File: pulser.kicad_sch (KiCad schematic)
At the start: 49 parts, among them J10 CONSMA002-SMD, J3 CONSMA002-SMD, J4 CONSMA002-SMD, J5 CONSMA002-SMD, J6 CONSMA002-SMD, J7 CONSMA002-SMD, J8 CONSMA002-SMD, J9 CONSMA002-SMD, U10 TLV9354IDR, U11 TLV9354IDR, U2 DSC1001DI2-125.0000T, U3 MAX14808ETK_

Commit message: DONE (inshallah)
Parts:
- added J16: External Power Connector, symbol Connector_Generic:Conn_02x08_Odd_Even
- added R128, R129, R130, R131, R132, R133, R134, R135: 90R 0805, symbol Device:R
- added TP1, TP2, TP3, TP4, TP5, TP53, TP54, TP55, TP56, TP57, TP58, TP59, TP6, TP60, TP7, TP8: RCT-0C, digikey-footprints:PROBE_PAD_0805, symbol dk_Test-Points:RCT-0C
- added TP10, TP11, TP12, TP13, TP14, TP15, TP16, TP9: TestPoint, symbol Connector:TestPoint
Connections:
- net TR_OUT1: now also R132.2; no longer R83.2, R84.1, U10.1 (OUT_A), U3.1 (LVOUT1)
- net TR_OUT2: now also R130.2; no longer R85.2, R86.1, U10.7 (OUT_B), U3.2 (LVOUT2)
- net TR_OUT3: now also R131.1; no longer R88.2, R90.1, U10.8 (OUT_C), U3.3 (LVOUT3)
- net TR_OUT4: now also R133.1; no longer R87.2, R89.1, U10.14 (OUT_D), U3.4 (LVOUT4)
- net TR_OUT5: now also R134.2; no longer R91.2, R93.1, U11.1 (OUT_A), U3.14 (LVOUT5)
- net TR_OUT6: now also R128.2; no longer R92.2, R94.1, U11.7 (OUT_B), U3.15 (LVOUT6)
- net TR_OUT7: now also R129.1; no longer R96.1, R98.2, U11.8 (OUT_C), U3.16 (LVOUT7)
- net TR_OUT8: now also R135.1; no longer R95.1, R97.2, U11.14 (OUT_D), U3.17 (LVOUT8)
- net VGNA: now also J16.1 (Pin_1), J16.2 (Pin_2), TP16.1
- net VGNB: now also J16.15 (Pin_15), J16.16 (Pin_16), TP9.1
- net VGPA: now also J16.3 (Pin_3), J16.4 (Pin_4), TP15.1
- net VGPB: now also J16.13 (Pin_13), J16.14 (Pin_14), TP10.1
- net VNNA: now also J16.7 (Pin_7), J16.8 (Pin_8), TP13.1
- net VNNB: now also J16.10 (Pin_10), J16.9 (Pin_9), TP12.1
- net VPPA: now also J16.5 (Pin_5), J16.6 (Pin_6), TP14.1
- net VPPB: now also J16.11 (Pin_11), J16.12 (Pin_12), TP11.1
- new net: R135.2, R95.1, TP58.1, U11.14 (OUT_D)
- new net: R130.1, R86.1, TP55.1, U10.7 (OUT_B)
- new net: R134.1, R93.1, TP57.1, U11.1 (OUT_A)
- new net: R133.2, R89.1, TP54.1, U10.14 (OUT_D)
- new net: R132.1, R84.1, TP53.1, U10.1 (OUT_A)
- new net: R131.2, R90.1, TP56.1, U10.8 (OUT_C)
- new net: R128.1, R94.1, TP59.1, U11.7 (OUT_B)
- new net: R129.2, R96.1, TP60.1, U11.8 (OUT_C)
- new net TR1: R83.2, TP1.1, U3.1 (LVOUT1)
- new net TR2: R85.2, TP2.1, U3.2 (LVOUT2)
- new net TR3: R88.2, TP3.1, U3.3 (LVOUT3)
- new net TR4: R87.2, TP4.1, U3.4 (LVOUT4)
- new net TR5: R91.2, TP5.1, U3.14 (LVOUT5)
- new net TR6: R92.2, TP6.1, U3.15 (LVOUT6)
- new net TR7: R98.2, TP7.1, U3.16 (LVOUT7)
- new net TR8: R97.2, TP8.1, U3.17 (LVOUT8)

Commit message: started layout, 20-30% done
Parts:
- added J18, J19, J20, J21, J22, J23, J24, J25: Conn_01x02_Pin, Connector_PinHeader_2.54mm:PinHeader_1x02_P2.54mm_Vertical, symbol Connector:Conn_01x02_Pin
- C1, C10, C11, C12, C2, C3, C4, C5, C6, C7, C8, C85, C86, C9: footprint (none) -> Capacitor_SMD:C_0603_1608Metric
- J16: footprint (none) -> Connector_PinHeader_2.54mm:PinHeader_2x08_P2.54mm_Vertical
- JP1, JP2, JP3, JP7: footprint (none) -> Jumper:SolderJumper-3_P1.3mm_Open_Pad1.0x1.5mm
- R128, R129, R130, R131, R132, R133, R134, R135, R48, R49, R50, R83, R84, R85, R86, R87, R88, R89, R90, R91, R92, R93, R94, R95, R96, R97, R98: footprint (none) -> Resistor_SMD:R_0603_1608Metric
- TP10, TP11, TP12, TP13, TP14, TP15, TP16, TP9: footprint (none) -> TestPoint:TestPoint_Pad_D1.5mm
- U10, U11: footprint SOIC_9354IDR_TEX -> TLV9354IDR:SOIC_9354IDR_TEX
- U2: footprint CDFN4_2P5X2_MCH -> DSC1001DI2-125.0000T:CDFN4_2P5X2_MCH
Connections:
- net GND: now also J18.2 (Pin_2), J19.2 (Pin_2), J20.2 (Pin_2), J21.2 (Pin_2), J22.2 (Pin_2), J23.2 (Pin_2), J24.2 (Pin_2), J25.2 (Pin_2)
- net HV_OUT3: now reaches J5.1, U3.47 (OUT3)
- net HV_OUT3: now also J20.1 (Pin_1)
- net HV_OUT1: now reaches J3.1, U3.51 (OUT1)
- net HV_OUT1: now also J18.1 (Pin_1)
- net HV_OUT2: now reaches J4.1, U3.49 (OUT2)
- net HV_OUT2: now also J19.1 (Pin_1)
- net HV_OUT6: now reaches J8.1, U3.39 (OUT6)
- net HV_OUT6: now also J23.1 (Pin_1)
- net HV_OUT8: now reaches J10.1, U3.35 (OUT8)
- net HV_OUT8: now also J25.1 (Pin_1)
- net HV_OUT7: now reaches J9.1, U3.37 (OUT7)
- net HV_OUT7: now also J24.1 (Pin_1)
- net HV_OUT5: now reaches J7.1, U3.41 (OUT5)
- net HV_OUT5: now also J22.1 (Pin_1)
- net HV_OUT4: now reaches J6.1, U3.45 (OUT4)
- net HV_OUT4: now also J21.1 (Pin_1)
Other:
- moved on the sheet: J10, J3, J4, J5, J6, J7, J8, J9

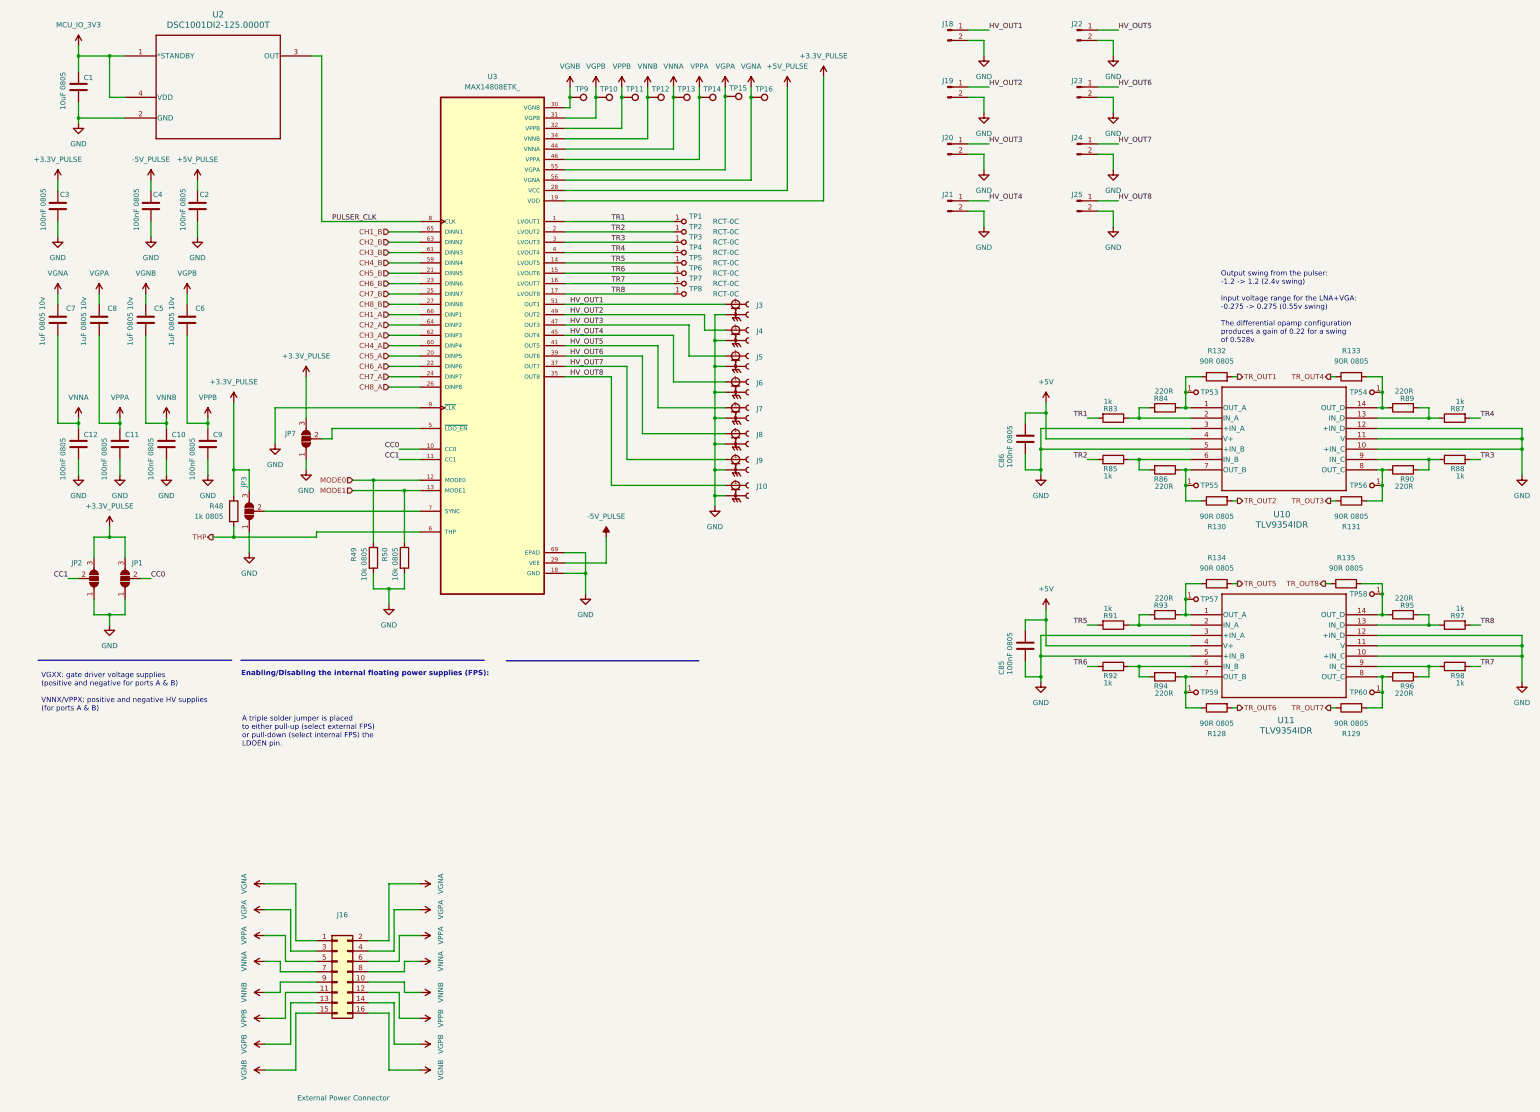
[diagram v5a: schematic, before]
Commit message: Finished placement & started routing, check on stackup & see routing & sigal integrity videos downloaded
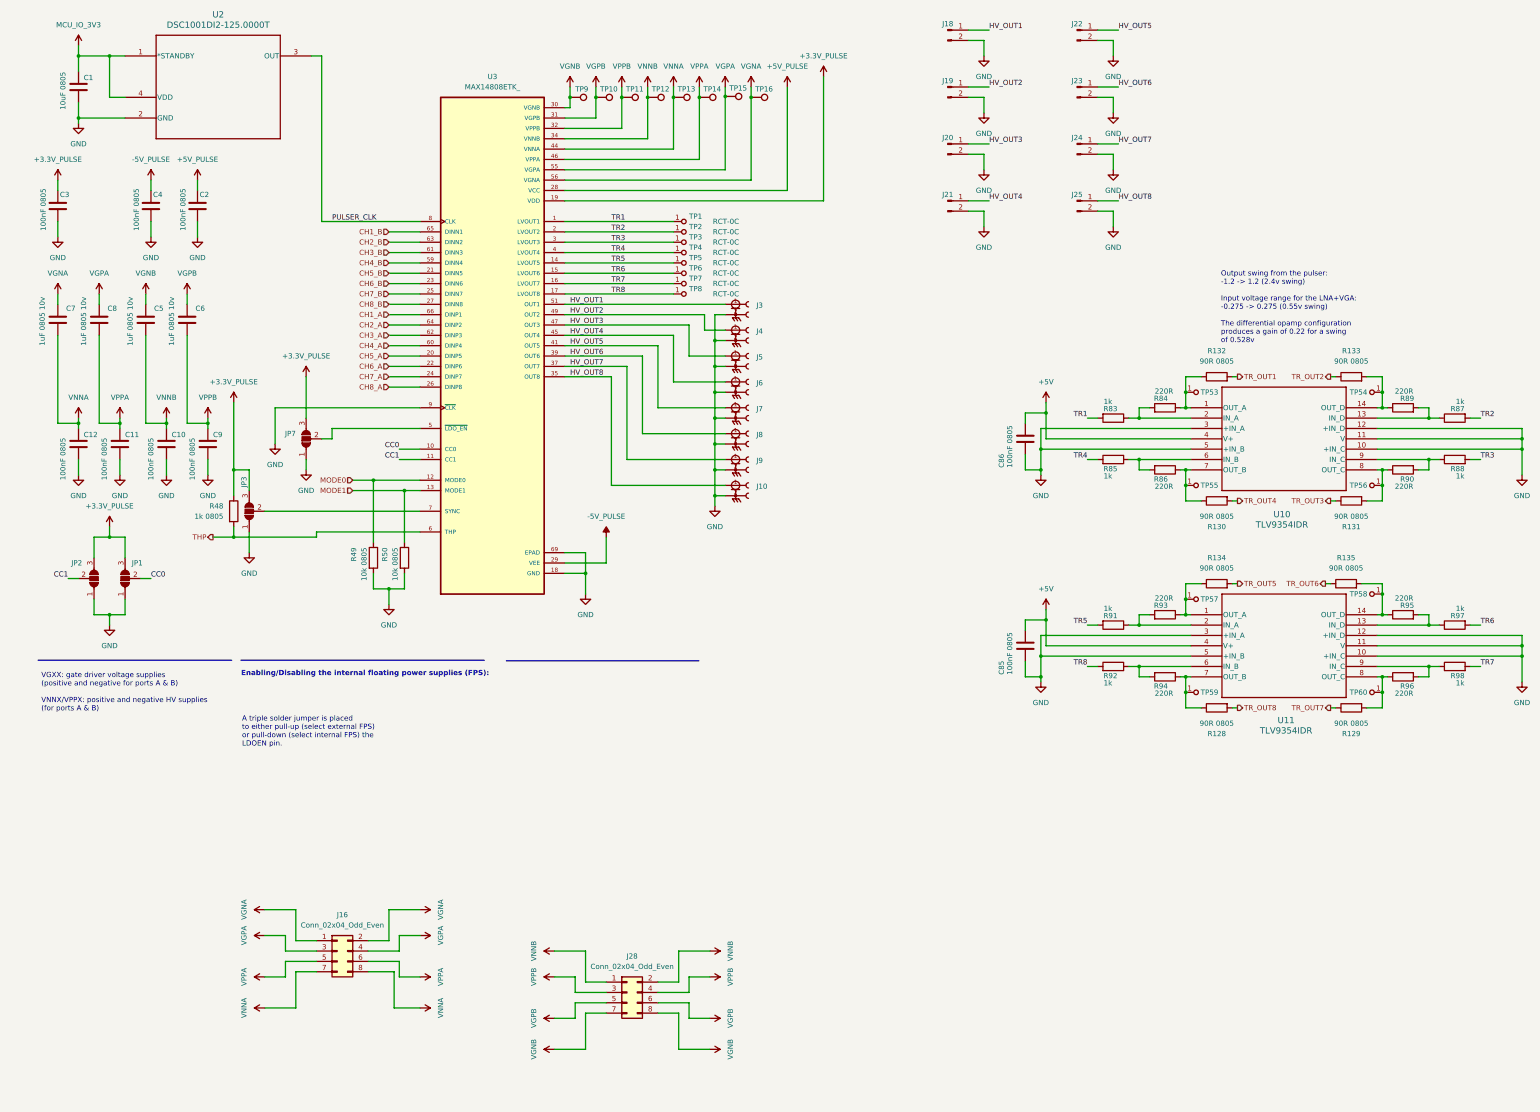
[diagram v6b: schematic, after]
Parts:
- removed J16: External Power Connector, Connector_PinHeader_2.54mm:PinHeader_2x08_P2.54mm_Vertical, symbol Connector_Generic:Conn_02x08_Odd_Even
- added J16, J28: Conn_02x04_Odd_Even, Connector_PinHeader_2.54mm:PinHeader_2x04_P2.54mm_Vertical, symbol Connector_Generic:Conn_02x04_Odd_Even
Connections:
- net TR2: now also R87.2; no longer R85.2
- net TR4: now also R85.2; no longer R87.2
- net TR6: now also R97.2; no longer R92.2
- net TR8: now also R92.2; no longer R97.2
- net TR_OUT2: now also R133.1; no longer R130.2
- net TR_OUT4: now also R130.2; no longer R133.1
- net TR_OUT6: now also R135.1; no longer R128.2
- net TR_OUT8: now also R128.2; no longer R135.1
- net VGNA: now also J16.1 (Pin_1), J16.2 (Pin_2)
- net VGNB: now also J28.7 (Pin_7), J28.8 (Pin_8)
- net VGPA: now also J16.3 (Pin_3), J16.4 (Pin_4)
- net VGPB: now also J28.5 (Pin_5), J28.6 (Pin_6)
- net VNNA: now also J16.7 (Pin_7), J16.8 (Pin_8)
- net VNNB: now also J28.1 (Pin_1), J28.2 (Pin_2)
- net VPPA: now also J16.5 (Pin_5), J16.6 (Pin_6)
- net VPPB: now also J28.3 (Pin_3), J28.4 (Pin_4)

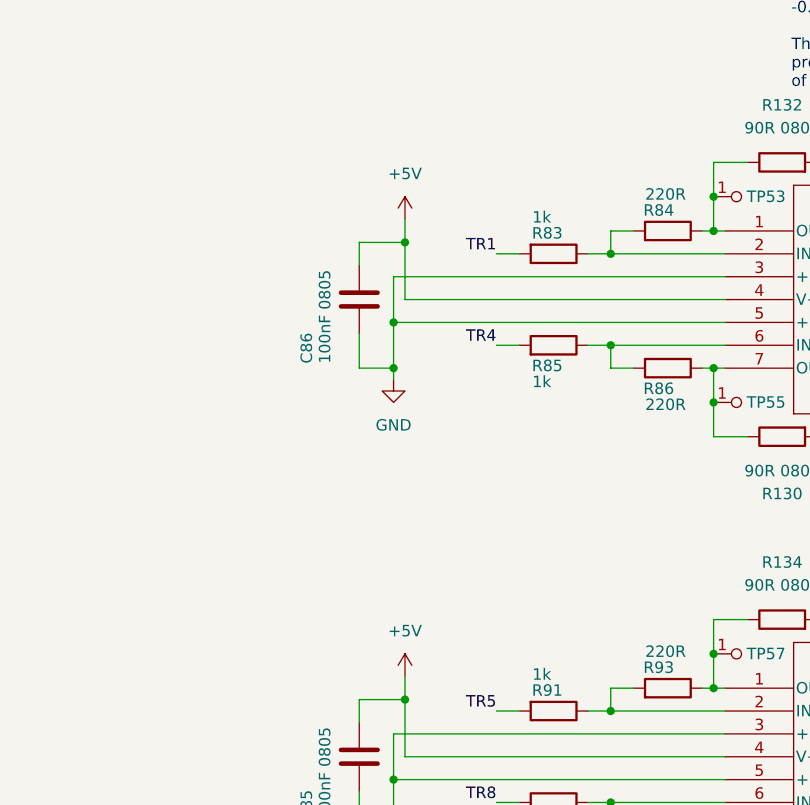
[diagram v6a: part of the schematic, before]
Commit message: 5% left, rearrange ADC channels for right AFE
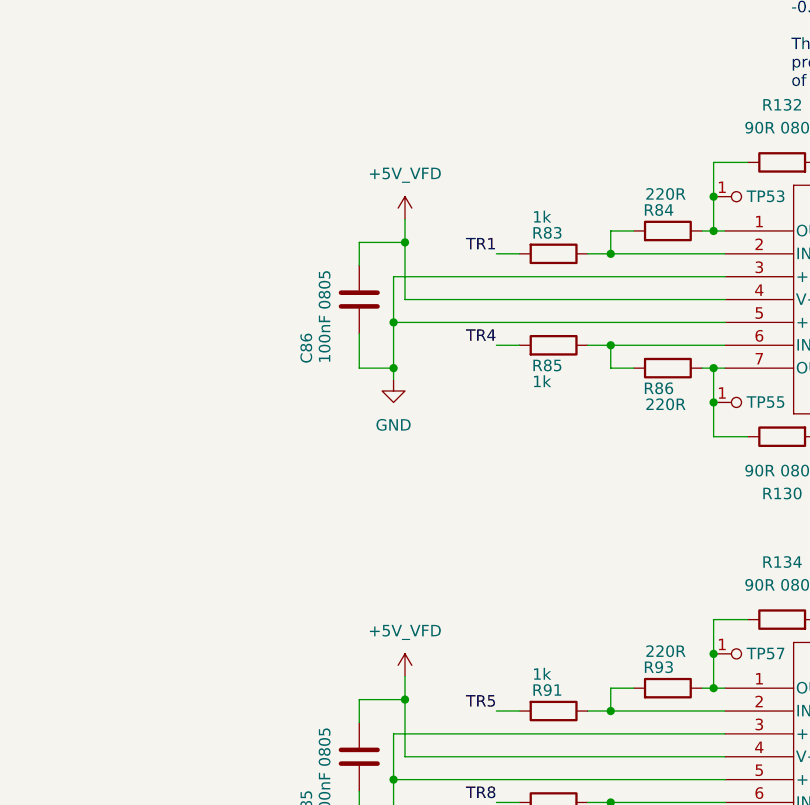
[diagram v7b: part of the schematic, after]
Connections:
- net +5V renamed +5V_VFD
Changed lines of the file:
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@@
 			)
 		)
-		(property "Value" "+5V"
+		(property "Value" "+5V_VFD"
 			(at 260.35 104.14 0)
 			(effects
@@
 			)
 		)
-		(property "Value" "+5V"
+		(property "Value" "+5V_VFD"
 			(at 260.35 154.94 0)
 			(effects

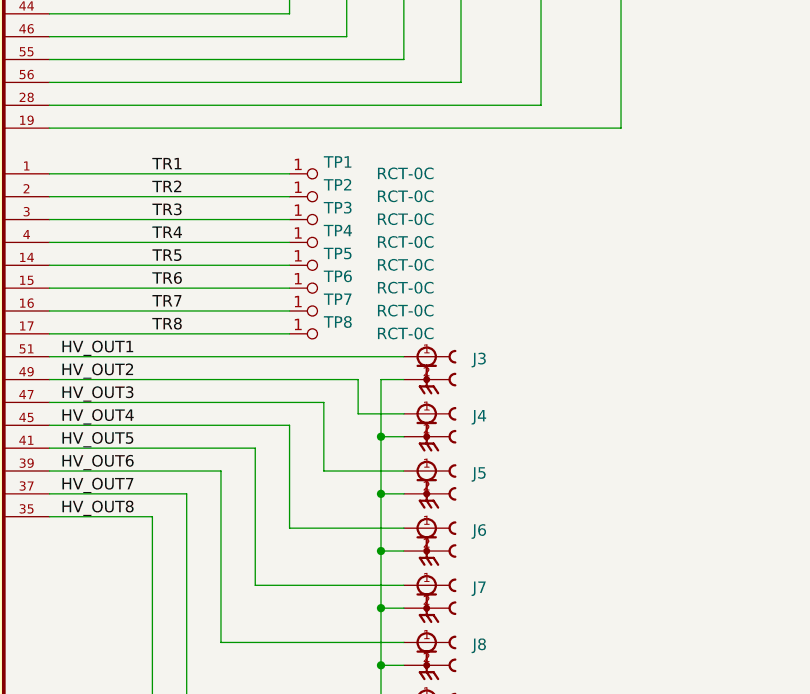
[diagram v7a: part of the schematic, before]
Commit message: added voltage monitoring, negative HV remaining & their routing + minimal editing
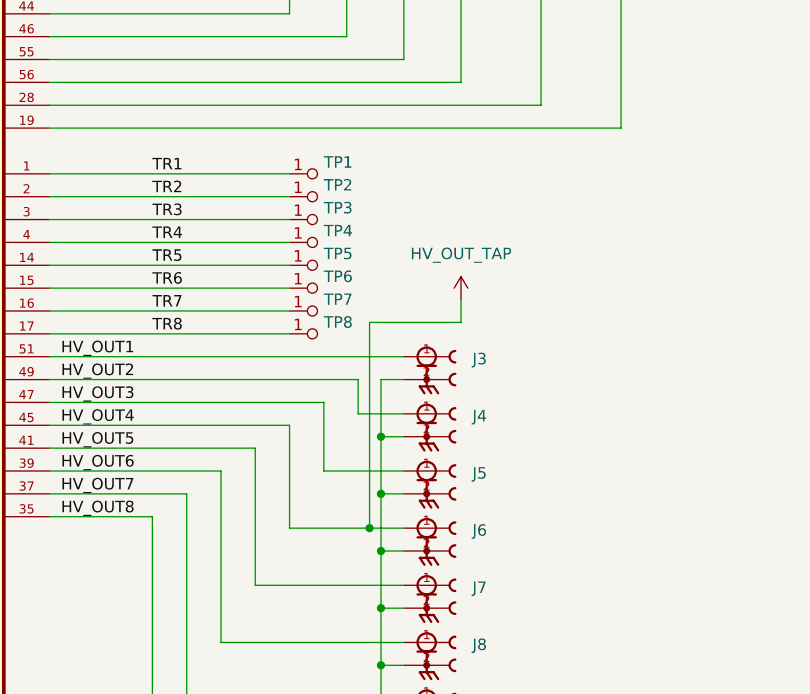
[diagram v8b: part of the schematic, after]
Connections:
- net HV_OUT4 renamed HV_OUT_TAP
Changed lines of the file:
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@@
 	)
 	(junction
+		(at 177.8 104.14)
+		(diameter 0)
+		(color 0 0 0 0)
+	)
+	(junction
 		(at 168.91 34.29)
 		(diameter 0)
@@
 	(wire
 		(pts
+			(xy 187.96 78.74) (xy 187.96 81.28)
+		)
+		(stroke
+			(width 0)
+			(type default)
+		)
+	)
+	(wire
+		(pts
 			(xy 241.3 59.69) (xy 246.38 59.69)
 		)
@@
 	(wire
 		(pts
-			(xy 168.91 104.14) (xy 181.61 104.14)
+			(xy 168.91 104.14) (xy 177.8 104.14)
 		)
 		(stroke
@@
 	(wire
 		(pts
+			(xy 187.96 81.28) (xy 177.8 81.28)
+		)
+		(stroke
+			(width 0)
+			(type default)
+		)
+	)
+	(wire
+		(pts
 			(xy 330.2 102.87) (xy 331.47 102.87)
 		)
@@
 	(wire
 		(pts
+			(xy 177.8 104.14) (xy 181.61 104.14)
+		)
+		(stroke
+			(width 0)
+			(type default)
+		)
+	)
+	(wire
+		(pts
 			(xy 99.06 105.41) (xy 106.68 105.41)
 		)
@@
 	(wire
 		(pts
+			(xy 177.8 81.28) (xy 177.8 104.14)
+		)
+		(stroke
+			(width 0)
+			(type default)
+		)
+	)
+	(wire
+		(pts
 			(xy 139.7 250.19) (xy 144.78 250.19)
 		)
@@
 				)
 				(justify right)
+				(hide yes)
 			)
 		)
@@
 				)
 				(justify right)
+				(hide yes)
 			)
 		)
@@
 				)
 				(justify right)
+				(hide yes)
 			)
 		)
@@
 				)
 				(justify right)
+				(hide yes)
 			)
 		)
@@
 				)
 				(justify right)
+				(hide yes)
 			)
 		)
@@
 				)
 				(justify right)
+				(hide yes)
 			)
 		)
@@
 				)
 				(justify right)
+				(hide yes)
 			)
 		)
@@
 				)
 				(justify right)
+				(hide yes)
 			)
 		)
@@
 					(unit 1)
 				)
+			)
+		)
+	)
+	(symbol
+		(lib_id "power:+3V0")
+		(at 187.96 78.74 0)
+		(unit 1)
+		(exclude_from_sim no)
+		(in_bom yes)
+		(on_board yes)
+		(dnp no)
+		(fields_autoplaced yes)
+		(property "Reference" "#PWR0183"
+			(at 187.96 82.55 0)
+			(effects
+				(font
+					(size 1.27 1.27)
+				)
+				(hide yes)
+			)
+		)
+		(property "Value" "HV_OUT_TAP"
+			(at 187.96 73.66 0)
+			(effects
+				(font
+					(size 1.27 1.27)
+				)
+			)
+		)
+		(property "Footprint" ""
+			(at 187.96 78.74 0)
+			(effects
+				(font
+					(size 1.27 1.27)
+				)
+				(hide yes)
+			)
+		)
+		(property "Datasheet" ""
+			(at 187.96 78.74 0)
+			(effects
+				(font
+					(size 1.27 1.27)
+				)
+				(hide yes)
+			)
+		)
+		(property "Description" "Power symbol creates a global label with name \"+3V0\""
+			(at 187.96 78.74 0)
+			(effects
+				(font
+					(size 1.27 1.27)
+				)
+				(hide yes)
+			)
+		)
+		(pin "1"
+		)
+		(instances
+			(project ""
+				(path "/9cc0bb16-a3df-40ec-93e8-11b5009319f1/3d58f5d9-3eeb-4243-b251-3f4dbba0d4d4"
+					(reference "#PWR0183")
+					(unit 1)
+				)
